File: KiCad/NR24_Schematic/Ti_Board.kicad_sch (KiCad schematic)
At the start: 24 parts, among them J5 AEM VDM (Vehicle Dynamics), J5 J1 Pin J3 Pin, J5 J12 (CAN Interface w/ Transce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, J5 J4 Pin J2 Pin, J5 J5 Pin J7 Pin, J5 J8 Pin J6 Pin, J5 XBEE PRO, J6 SpeakON_NL2, Q1 Q_NMOS_DGS, Q2 Q_NMOS_DGS, Q3 Q_NMOS_DGS

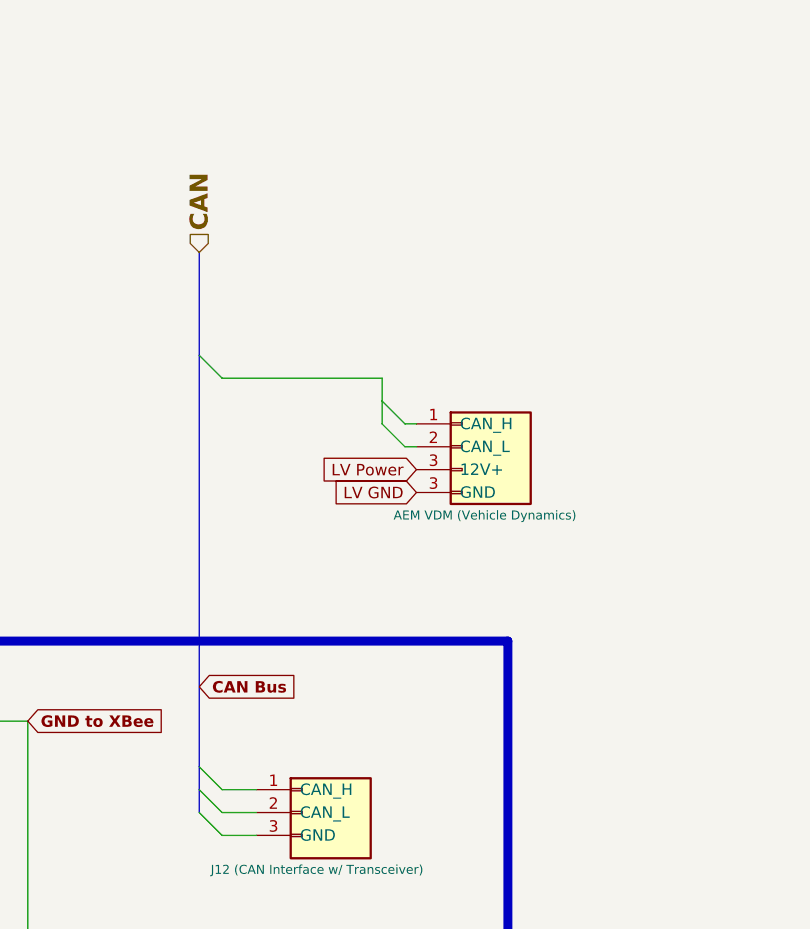
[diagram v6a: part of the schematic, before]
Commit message: Revert "Update Ti_Board.kicad_sch"
This reverts commit 827dd6d678deb170c15ae9c5bc81964bdf1e9ab9.
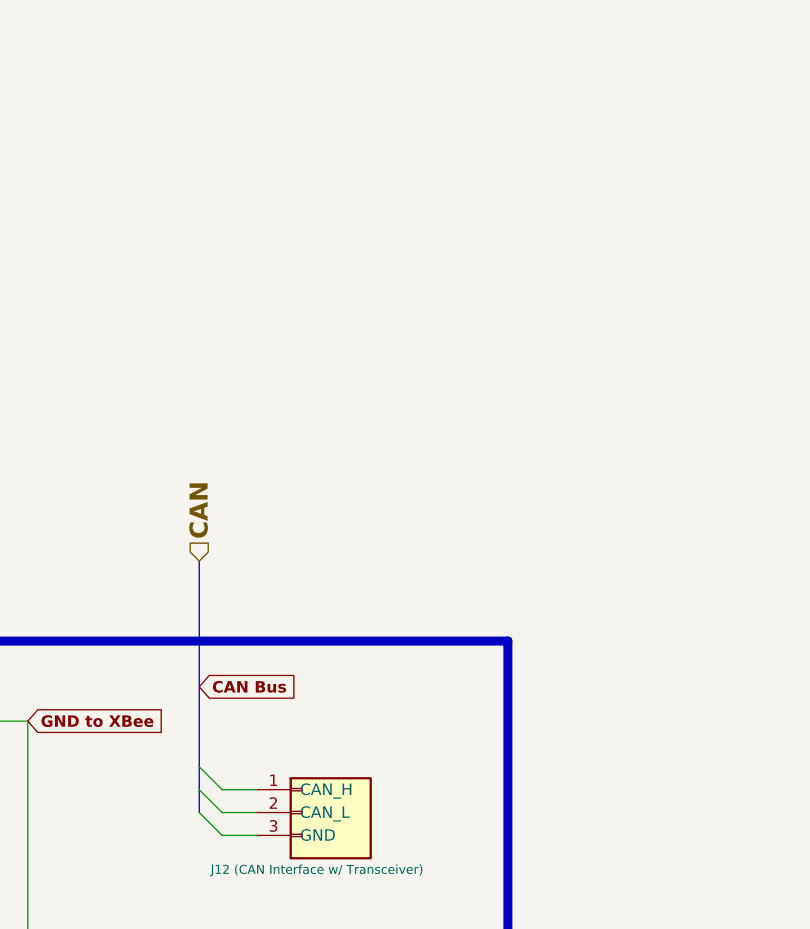
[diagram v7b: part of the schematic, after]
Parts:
- removed J5: AEM VDM (Vehicle Dynamics), symbol Connector_Generic:Conn_02x06_Counter_Clockwise
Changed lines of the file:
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@@
     (stroke (width 0) (type default))
-  )
-  (bus_entry (at 308.61 99.06) (size 2.54 2.54)
-    (stroke (width 0.75) (type default) (color 0 132 132 1))
   )
   (bus_entry (at 66.04 149.86) (size -2.54 2.54)
@@
     (stroke (width 0) (type default))
   )
-  (bus_entry (at 288.29 93.98) (size 2.54 2.54)
-    (stroke (width 0.75) (type default) (color 0 132 132 1))
-  )
   (bus_entry (at 127 132.08) (size -2.54 2.54)
     (stroke (width 0) (type default))
   )
-  (bus_entry (at 308.61 101.6) (size 2.54 2.54)
-    (stroke (width 0.75) (type default) (color 0 132 132 1))
-  )
   (bus_entry (at 92.71 142.24) (size 2.54 2.54)
     (stroke (width 0) (type default))
@@
   (wire (pts (xy 280.67 203.2) (xy 180.34 203.2))
     (stroke (width 0) (type default))
-  )
-  (wire (pts (xy 290.83 96.52) (xy 308.61 96.52))
-    (stroke (width 0.75) (type default) (color 0 132 132 1))
   )
   (wire (pts (xy 33.02 134.62) (xy 34.29 134.62))
@@
     (stroke (width 0) (type default))
   )
-  (wire (pts (xy 308.61 99.06) (xy 308.61 101.6))
-    (stroke (width 0.75) (type default) (color 0 132 132 1))
-  )
   (wire (pts (xy 33.02 142.24) (xy 34.29 142.24))
     (stroke (width 0) (type default))
@@
     (stroke (width 0) (type default))
   )
-  (wire (pts (xy 308.61 99.06) (xy 308.61 96.52))
+  (wire (pts (xy 123.19 144.78) (xy 124.46 144.78))
+    (stroke (width 0) (type default))
+  )
+  (wire (pts (xy 62.23 147.32) (xy 63.5 147.32))
+    (stroke (width 0) (type default))
+  )
+  (wire (pts (xy 104.14 59.69) (xy 101.6 59.69))
+    (stroke (width 0) (type default))
+  )
+  (wire (pts (xy 182.88 134.62) (xy 182.88 201.93))
+    (stroke (width 0) (type default))
+  )
+  (wire (pts (xy 111.76 59.69) (xy 121.92 59.69))
+    (stroke (width 0) (type default))
+  )
+  (wire (pts (xy 123.19 142.24) (xy 124.46 142.24))
+    (stroke (width 0) (type default))
+  )
+  (wire (pts (xy 121.92 81.28) (xy 121.92 80.01))
+    (stroke (width 0) (type default))
+  )
+  (wire (pts (xy 123.19 154.94) (xy 124.46 154.94))
+    (stroke (width 0) (type default))
+  )
+  (bus (pts (xy 220.98 262.89) (xy 220.98 280.67))
+    (stroke (width 0) (type default))
+  )
+  (wire (pts (xy 147.32 80.01) (xy 172.72 80.01))
+    (stroke (width 0) (type default))
+  )
+  (wire (pts (xy 181.61 204.47) (xy 281.94 204.47))
+    (stroke (width 0) (type default))
+  )
+  (wire (pts (xy 62.23 152.4) (xy 63.5 152.4))
+    (stroke (width 0) (type default))
+  )
+  (wire (pts (xy 205.74 99.06) (xy 232.41 99.06))
+    (stroke (width 0) (type default))
+  )
+  (wire (pts (xy 232.41 152.4) (xy 232.41 99.06))
+    (stroke (width 0) (type default))
+  )
+  (wire (pts (xy 33.02 149.86) (xy 34.29 149.86))
+    (stroke (width 0) (type default))
+  )
+  (wire (pts (xy 177.8 50.8) (xy 182.88 50.8))
+    (stroke (width 0) (type default))
+  )
+  (wire (pts (xy 205.74 99.06) (xy 205.74 71.12))
+    (stroke (width 0) (type default))
+  )
+  (wire (pts (xy 95.25 137.16) (xy 96.52 137.16))
+    (stroke (width 0) (type default))
+  )
+  (wire (pts (xy 62.23 142.24) (xy 63.5 142.24))
+    (stroke (width 0) (type default))
+  )
+  (wire (pts (xy 33.02 152.4) (xy 34.29 152.4))
+    (stroke (width 0) (type default))
+  )
+  (wire (pts (xy 62.23 157.48) (xy 63.5 157.48))
+    (stroke (width 0) (type default))
+  )
+  (wire (pts (xy 182.88 134.62) (xy 186.69 134.62))
+    (stroke (width 0) (type default))
+  )
+  (bus (pts (xy 288.29 116.84) (xy 288.29 139.7))
     (stroke (width 0.75) (type default) (color 0 132 132 1))
   )
-  (wire (pts (xy 123.19 144.78) (xy 124.46 144.78))
-    (stroke (width 0) (type default))
-  )
-  (wire (pts (xy 62.23 147.32) (xy 63.5 147.32))
-    (stroke (width 0) (type default))
-  )
-  (wire (pts (xy 104.14 59.69) (xy 101.6 59.69))
-    (stroke (width 0) (type default))
-  )
-  (wire (pts (xy 182.88 134.62) (xy 182.88 201.93))
-    (stroke (width 0) (type default))
-  )
-  (wire (pts (xy 111.76 59.69) (xy 121.92 59.69))
-    (stroke (width 0) (type default))
-  )
-  (wire (pts (xy 123.19 142.24) (xy 124.46 142.24))
-    (stroke (width 0) (type default))
-  )
-  (wire (pts (xy 121.92 81.28) (xy 121.92 80.01))
-    (stroke (width 0) (type default))
-  )
-  (wire (pts (xy 123.19 154.94) (xy 124.46 154.94))
-    (stroke (width 0) (type default))
-  )
-  (bus (pts (xy 220.98 262.89) (xy 220.98 280.67))
-    (stroke (width 0) (type default))
-  )
-  (wire (pts (xy 147.32 80.01) (xy 172.72 80.01))
-    (stroke (width 0) (type default))
-  )
-  (wire (pts (xy 181.61 204.47) (xy 281.94 204.47))
-    (stroke (width 0) (type default))
-  )
-  (wire (pts (xy 62.23 152.4) (xy 63.5 152.4))
-    (stroke (width 0) (type default))
-  )
-  (wire (pts (xy 205.74 99.06) (xy 232.41 99.06))
-    (stroke (width 0) (type default))
-  )
-  (wire (pts (xy 232.41 152.4) (xy 232.41 99.06))
-    (stroke (width 0) (type default))
-  )
-  (wire (pts (xy 33.02 149.86) (xy 34.29 149.86))
-    (stroke (width 0) (type default))
-  )
-  (wire (pts (xy 177.8 50.8) (xy 182.88 50.8))
-    (stroke (width 0) (type default))
-  )
-  (wire (pts (xy 205.74 99.06) (xy 205.74 71.12))
-    (stroke (width 0) (type default))
-  )
-  (wire (pts (xy 95.25 137.16) (xy 96.52 137.16))
-    (stroke (width 0) (type default))
-  )
-  (wire (pts (xy 62.23 142.24) (xy 63.5 142.24))
-    (stroke (width 0) (type default))
-  )
-  (wire (pts (xy 33.02 152.4) (xy 34.29 152.4))
-    (stroke (width 0) (type default))
-  )
-  (wire (pts (xy 62.23 157.48) (xy 63.5 157.48))
-    (stroke (width 0) (type default))
-  )
-  (wire (pts (xy 182.88 134.62) (xy 186.69 134.62))
-    (stroke (width 0) (type default))
-  )
-  (bus (pts (xy 288.29 82.55) (xy 288.29 93.98))
-    (stroke (width 0.75) (type default) (color 0 132 132 1))
-  )
   (wire (pts (xy 180.34 203.2) (xy 180.34 142.24))
     (stroke (width 0) (type default))
   )
-  (bus (pts (xy 288.29 93.98) (xy 288.29 139.7))
-    (stroke (width 0.75) (type default) (color 0 132 132 1))
-  )
   (wire (pts (xy 121.92 80.01) (xy 147.32 80.01))
     (stroke (width 0) (type default))
@@
     (stroke (width 0) (type default))
   )
-  (wire (pts (xy 311.15 101.6) (xy 312.42 101.6))
-    (stroke (width 0) (type default))
-  )
   (wire (pts (xy 95.25 154.94) (xy 96.52 154.94))
     (stroke (width 0) (type default))
@@
   )
   (wire (pts (xy 95.25 144.78) (xy 96.52 144.78))
-    (stroke (width 0) (type default))
-  )
-  (wire (pts (xy 311.15 104.14) (xy 312.42 104.14))
     (stroke (width 0) (type default))
   )
@@
     )
   )
-  (global_label "LV Power" (shape input) (at 312.42 106.68 180) (fields_autoplaced)
-    (effects (font (size 1.27 1.27)) (justify right))
-    (property "Intersheetrefs" "${INTERSHEET_REFS}" (at 300.7262 106.68 0)
-      (effects (font (size 1.27 1.27)) (justify right) hide)
-    )
-  )
   (global_label "BoosterXL" (shape input) (at 127 144.78 0) (fields_autoplaced)
     (effects (font (size 1.27 1.27) (thickness 0.254) bold) (justify left))
@@
     )
   )
-  (global_label "LV GND" (shape input) (at 312.42 109.22 180) (fields_autoplaced)
-    (effects (font (size 1.27 1.27)) (justify right))
-    (property "Intersheetrefs" "${INTERSHEET_REFS}" (at 302.48 109.22 0)
-      (effects (font (size 1.27 1.27)) (justify right) hide)
-    )
-  )
   (global_label "BoosterXL" (shape input) (at 92.71 134.62 180) (fields_autoplaced)
     (effects (font (size 1.27 1.27) (thickness 0.254) bold) (justify right))
@@
     )
   )
-  (hierarchical_label "CAN" (shape input) (at 288.29 82.55 90) (fields_autoplaced)
+  (hierarchical_label "CAN" (shape input) (at 288.29 116.84 90) (fields_autoplaced)
     (effects (font (size 2 2) (thickness 0.4) bold (color 0 194 194 1)) (justify left))
   )
@@
         )
       )
-    )
-  )
-  (symbol (lib_name "Conn_02x06_Counter_Clockwise_9") (lib_id "Connector_Generic:Conn_02x06_Counter_Clockwise") (at 327.66 107.95 0) (unit 1)
-    (in_bom yes) (on_board yes) (dnp no)
-    (property "Reference" "J5" (at 313.69 119.38 90)
-      (effects (font (size 1.27 1.27)) (justify right) hide)
-    )
-    (property "Value" "AEM VDM (Vehicle Dynamics)" (at 309.88 111.76 0)
-      (effects (font (size 1 1)) (justify left))
-    )
-    (property "Footprint" "" (at 317.5 106.68 0)
-      (effects (font (size 1.27 1.27)) hide)
-    )
-    (property "Datasheet" "~" (at 317.5 107.95 0)
-      (effects (font (size 1.27 1.27)) hide)
-    )
-    (pin "1")
-    (pin "2")
-    (pin "3")
-    (pin "3")
-    (instances
-      (project "Car_TractiveSystem_v2"
-        (path "/588b5c14-1813-4e1d-9dbe-940839ecebe3"
-          (reference "J5") (unit 1)
-        )
-        (path "/588b5c14-1813-4e1d-9dbe-940839ecebe3/42103732-fa28-467e-b394-54af70cbf903"
-          (reference "J3") (unit 1)
-        )
-      )
-      (project "Ti_Board"
-        (path "/95cd4c17-85c0-46ed-9908-1b2dc6d240f0"
-          (reference "J4") (unit 1)
-        )
-      )

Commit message: Now it is pretty :)
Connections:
- net Rocker GRN is gone; now on net To Dash: J5.73 (GPIO15), R4.1
- net BLCK GND renamed Low input
- net Ready to Drive Speaker (+) renamed Ready to Drive Speaker
- net Rocker BLK renamed To Dash
- net in_BLK renamed BLK
